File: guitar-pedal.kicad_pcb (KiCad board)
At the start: 2 copper layers, 52.1 x 107.9 mm, 50 parts, among them J1 USB_OTG, J2 AudioJack2, J3 AudioJack2, J4 Test_Headers, SW1 SW_SPDT, SW2 SW_3PDT, SW3 Boot, SW4 Reset, SW5 SW_Push_SPDT, SW6 SW_Push_SPDT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

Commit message: start ground pour
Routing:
- net +3V3: track 271.4 -> 266.0 mm
- net Net-(SW5-Pad2): track 74.3 -> 71.2 mm
- net Net-(SW6-Pad2): track 80.6 -> 78.1 mm
- net Net-(D1-Pad1): track 32.0 -> 31.4 mm
- net GND: vias 0 -> 15
- added copper zone on B.Cu, net GND
- added copper zone on F.Cu, net GND

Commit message: done with layout submission :O
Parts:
- moved C20 3.46 mm to (124.7, 124.6)
- moved C11 1.73 mm to (156.8, 113.1), turned to 90 degrees
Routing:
- net Net-(J1-Pad1): track 131.8 -> 127.2 mm
- net GND: track 0.00 -> 3.76 mm, vias 15 -> 28
- net Net-(C20-Pad1): track 7.88 -> 4.43 mm
- net /CODEC_DATA_OUT: track 65.1 -> 62.3 mm
- net /CODEC_BITCLK: track 76.4 -> 73.7 mm
- net /RAW_OUT: track 115.4 -> 116.4 mm
- net Net-(C8-Pad1): track 42.0 -> 41.4 mm

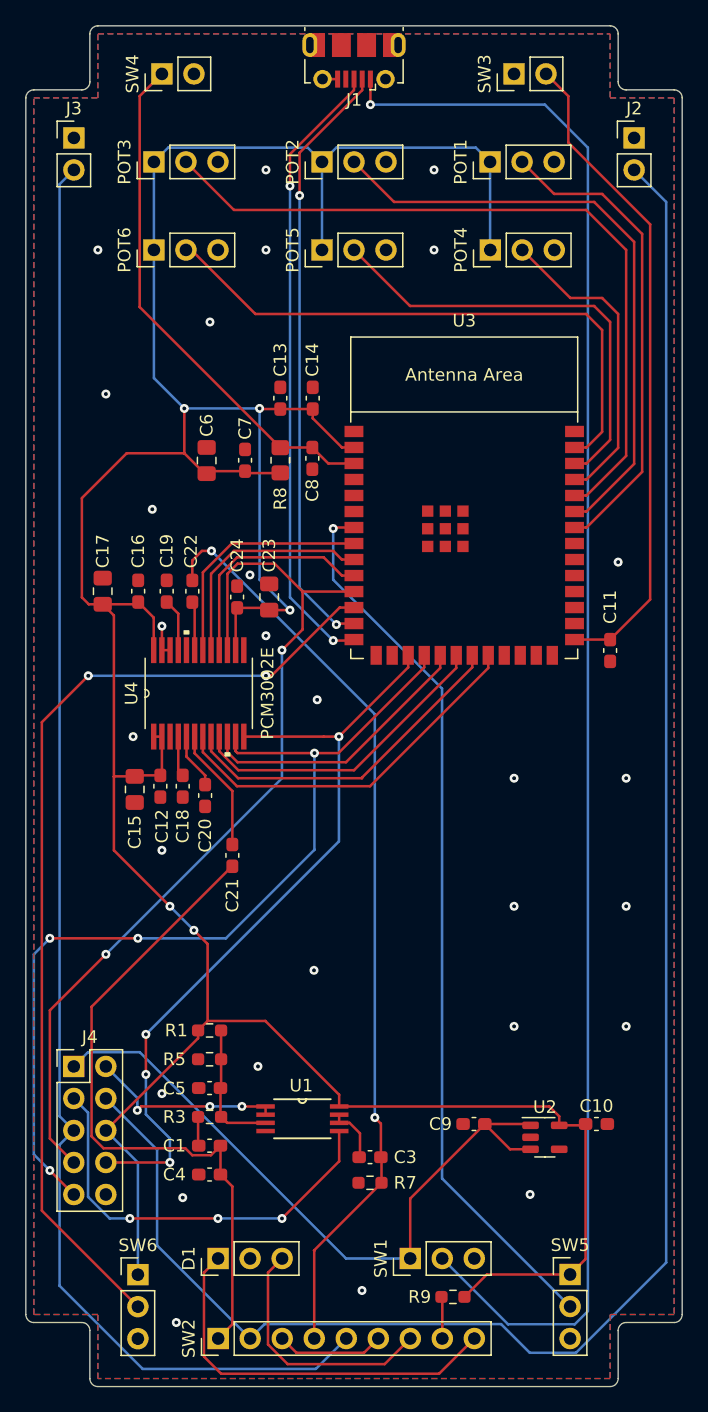
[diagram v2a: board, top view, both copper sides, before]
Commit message: add back silkscreen
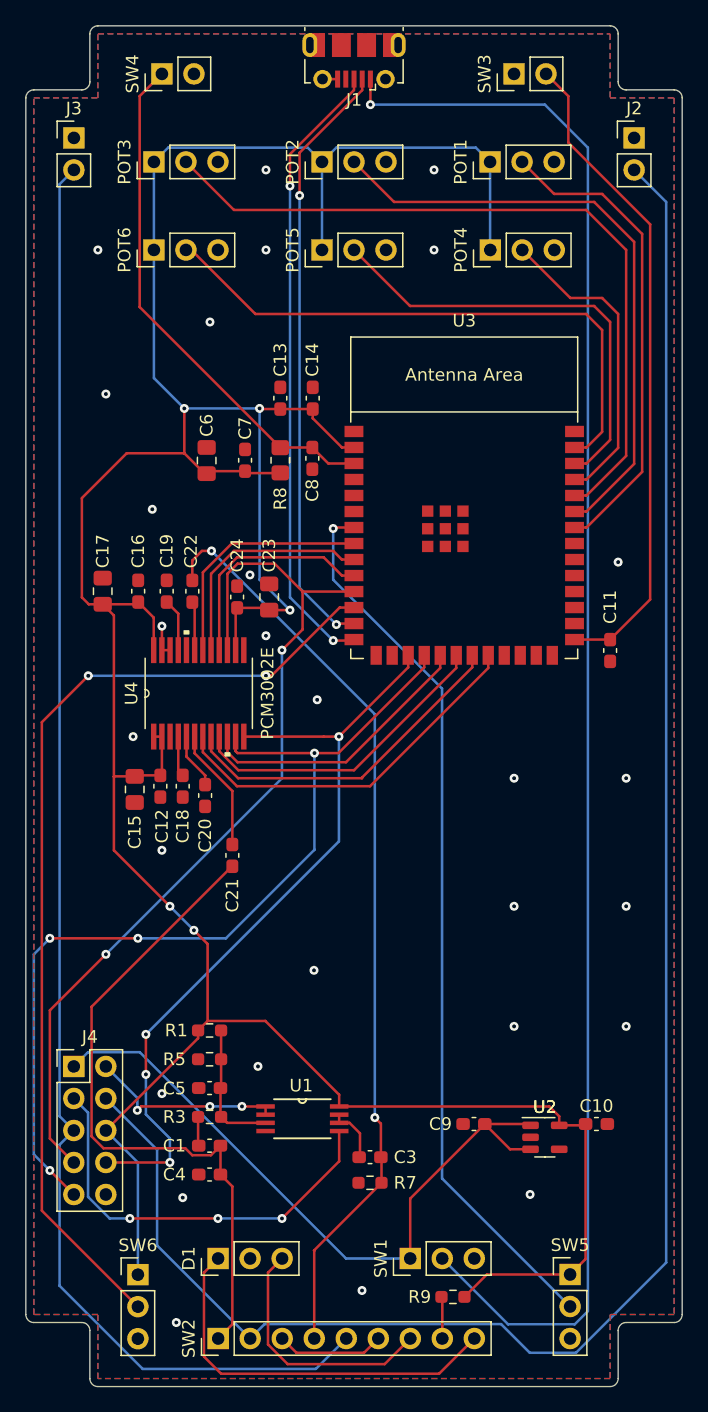
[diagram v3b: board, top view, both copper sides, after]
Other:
- board text added: "D1"
- board text added: "J1"
- board text added: "J2"
- board text added: "J3"
- board text added: "J4"
- board text added: "POT1"
- board text added: "POT2"
- board text added: "POT3"
- board text added: "POT4"
- board text added: "POT5"
- board text added: "POT6"
- board text added: "SW1"
- board text added: "SW2"
- board text added: "SW3"
- board text added: "SW4"
- board text added: "SW5"
- board text added: "SW6"
- board text added: "U2"
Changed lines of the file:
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@@
     (property "Sheetname" "")
     (attr through_hole)
-    (fp_text reference "D1" (at 0 -2.33 90) (layer "F.SilkS")
-      (effects (font (size 1 1) (thickness 0.15)))
+    (fp_text reference "D1" (at 0 -2.33 90) (layer "B.SilkS")
+      (effects (font (size 1 1) (thickness 0.15)) (justify mirror))
     )
     (fp_text value "LED_Dual_AKA" (at 0 7.41 90) (layer "F.Fab")
@@
     (property "Sheetname" "")
     (attr through_hole)
-    (fp_text reference "J2" (at 0 -2.33) (layer "F.SilkS")
-      (effects (font (size 1 1) (thickness 0.15)))
+    (fp_text reference "J2" (at 0 -2.33) (layer "B.SilkS")
+      (effects (font (size 1 1) (thickness 0.15)) (justify mirror))
     )
     (fp_text value "AudioJack2" (at -0.635 5.207) (layer "F.Fab")
@@
     (property "Sheetname" "")
     (attr through_hole)
-    (fp_text reference "J4" (at 1.27 -2.33) (layer "F.SilkS")
-      (effects (font (size 1 1) (thickness 0.15)))
+    (fp_text reference "J4" (at 1.27 -2.33) (layer "B.SilkS")
+      (effects (font (size 1 1) (thickness 0.15)) (justify mirror))
     )
     (fp_text value "Test_Headers" (at -2.789 5.075 90) (layer "F.Fab")
@@
   (gr_line (start 116.205 63.5) (end 156.845 63.5) (layer "Edge.Cuts") (width 0.1))
   (gr_line (start 157.48 64.135) (end 157.48 67.945) (layer "Edge.Cuts") (width 0.1))
+  (gr_text "POT5" (at 131.6482 81.28 90) (layer "B.SilkS")
+    (effects (font (size 1 1) (thickness 0.15)) (justify mirror))
+  )
+  (gr_text "POT1" (at 144.9832 74.295 90) (layer "B.SilkS")
+    (effects (font (size 1 1) (thickness 0.15)) (justify mirror))
+  )
+  (gr_text "POT4" (at 145.0086 81.28 90) (layer "B.SilkS")
+    (effects (font (size 1 1) (thickness 0.15)) (justify mirror))
+  )
+  (gr_text "SW1" (at 138.6586 161.29 90) (layer "B.SilkS")
+    (effects (font (size 1 1) (thickness 0.15)) (justify mirror))
+  )
+  (gr_text "SW6" (at 119.38 160.2486) (layer "B.SilkS")
+    (effects (font (size 1 1) (thickness 0.15)) (justify mirror))
+  )
+  (gr_text "J3" (at 114.3 70.0532) (layer "B.SilkS")
+    (effects (font (size 1 1) (thickness 0.15)) (justify mirror))
+  )
+  (gr_text "POT6" (at 118.3132 81.28 90) (layer "B.SilkS")
+    (effects (font (size 1 1) (thickness 0.15)) (justify mirror))
+  )
+  (gr_text "J1" (at 136.525 69.3674) (layer "B.SilkS")
+    (effects (font (size 1 1) (thickness 0.15)) (justify mirror))
+  )
+  (gr_text "POT3" (at 118.3132 74.295 90) (layer "B.SilkS")
+    (effects (font (size 1 1) (thickness 0.15)) (justify mirror))
+  )
+  (gr_text "SW4" (at 118.9736 67.31 90) (layer "B.SilkS")
+    (effects (font (size 1 1) (thickness 0.15)) (justify mirror))
+  )
+  (gr_text "POT2" (at 131.6482 74.295 90) (layer "B.SilkS")
+    (effects (font (size 1 1) (thickness 0.15)) (justify mirror))
+  )
+  (gr_text "SW5" (at 153.67 160.2232) (layer "B.SilkS")
+    (effects (font (size 1 1) (thickness 0.15)) (justify mirror))
+  )
+  (gr_text "SW3" (at 146.8882 67.31 90) (layer "B.SilkS")
+    (effects (font (size 1 1) (thickness 0.15)) (justify mirror))
+  )
+  (gr_text "SW2" (at 123.4186 167.64 90) (layer "B.SilkS")
+    (effects (font (size 1 1) (thickness 0.15)) (justify mirror))
+  )
+  (gr_text "D1" (at 123.4186 161.29 90) (layer "F.SilkS")
+    (effects (font (size 1 1) (thickness 0.15)))
+  )
+  (gr_text "U2" (at 151.6634 149.2758) (layer "F.SilkS")
+    (effects (font (size 1 1) (thickness 0.15)))
+  )
+  (gr_text "J4" (at 115.57 143.7132) (layer "F.SilkS")
+    (effects (font (size 1 1) (thickness 0.15)))
+  )
+  (gr_text "J2" (at 158.75 70.0532) (layer "F.SilkS")
+    (effects (font (size 1 1) (thickness 0.15)))
+  )
   (segment (start 124.156 152.294001) (end 124.206 152.344001) (width 0.2032) (layer "F.Cu") (net 1))
   (segment (start 124.156 150.058001) (end 124.156 152.294001) (width 0.2032) (layer "F.Cu") (net 1))

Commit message: Fix switch to ground
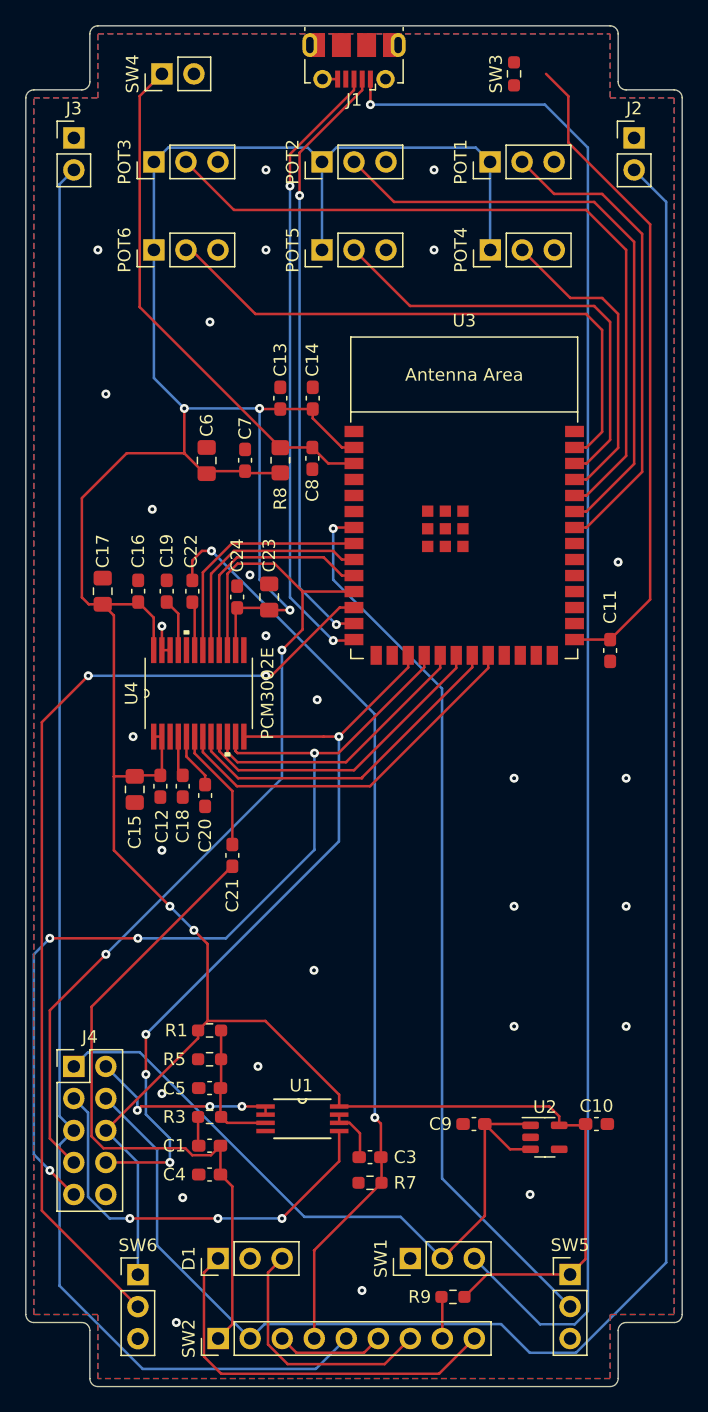
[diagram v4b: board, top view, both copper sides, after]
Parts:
- SW3: footprint Connector_PinHeader_2.54mm:PinHeader_1x02_P2.54mm_Vertical -> Resistor_SMD:R_0603_1608Metric_Pad0.98x0.95mm_HandSolder
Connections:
- SW1 pad 1: +5V -> GND
- SW1 pad 2: Net-(J1-Pad1) -> +5V
- SW1 pad 3: unconnected-(SW1-Pad3) -> Net-(J1-Pad1)
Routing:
- net Net-(J1-Pad1): track 127.2 -> 124.6 mm
- net +5V: track 55.2 -> 56.7 mm
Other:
- board text removed: "U2"

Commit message: Change trace width, move usb
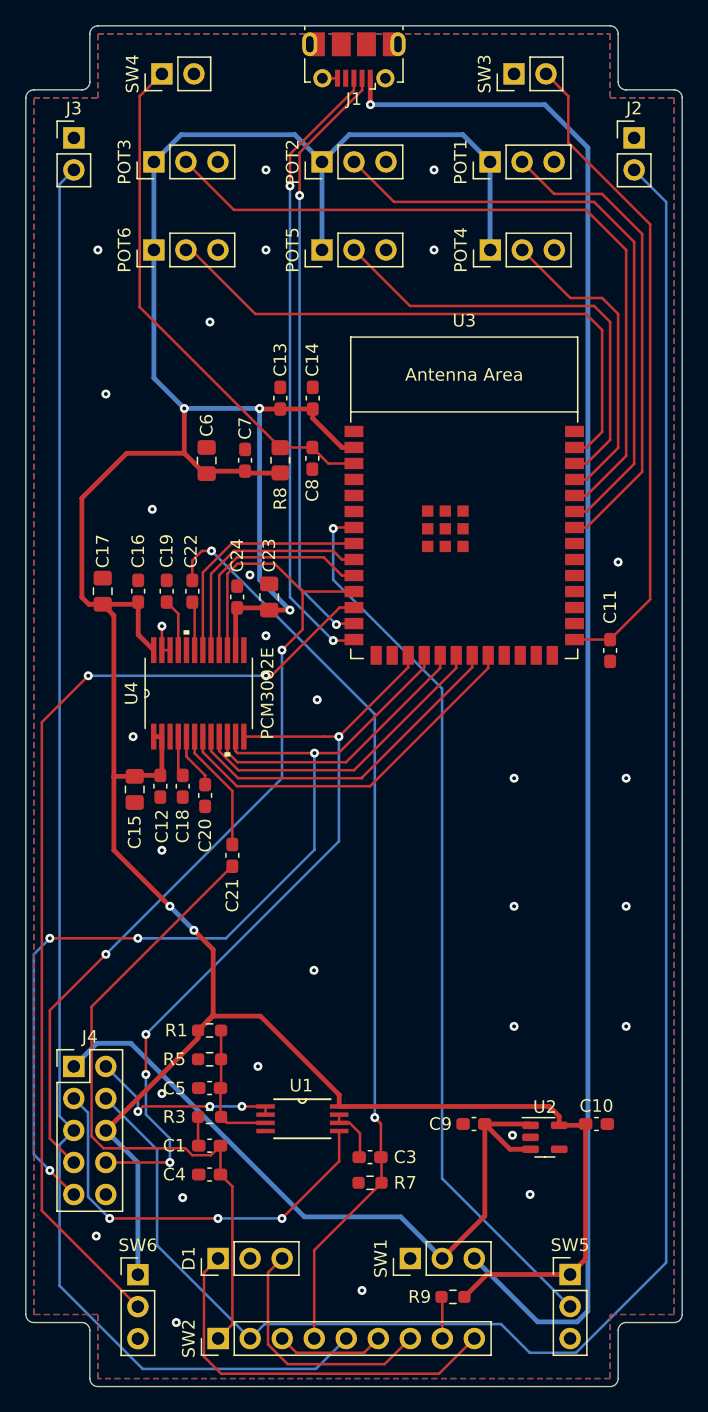
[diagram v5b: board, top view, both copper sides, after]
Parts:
- SW3: footprint Resistor_SMD:R_0603_1608Metric_Pad0.98x0.95mm_HandSolder -> Connector_PinHeader_2.54mm:PinHeader_1x02_P2.54mm_Vertical
- moved J1 0.06 mm to (136.5, 66.2)
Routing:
- net +3V3: track 266.0 -> 268.4 mm
- net +5V: track 56.7 -> 57.3 mm
- net GND: vias 28 -> 30
